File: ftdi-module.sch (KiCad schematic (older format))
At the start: 21 parts

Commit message: FTDI module complete
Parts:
- added 1V8_FT, 3V3, 5V0: TP_SMD1MM, antmicro-footprints:Testpoint_smd_1mm, symbol antmicroTestPoints:TP_SMD1MM
- added C? (x4): C_3u3_0402, antmicro-footprints:0402-cap, symbol antmicroCapacitors0402:C_3u3_0402
- added C? (x2): C_100n_0402, antmicro-footprints:0402-cap, symbol antmicroCapacitors0402:C_100n_0402
- added C? (x2): C_1u_0402, antmicro-footprints:0402-cap, symbol antmicroCapacitors0402:C_1u_0402
- added D?: PESD5V0S2BQA, antmicro-footprints:TPD2E009DRTR, symbol antmicroTVSDiodes:PESD5V0S2BQA
- added D?: KP-1608CGCK, antmicro-footprints:LED_0603, symbol antmicroLEDIndicationDiscrete:KP-1608CGCK
- added FB?: BLM18AG601SN1D, antmicro-footprints:0603, symbol antmicroFerriteBeadsandChips:BLM18AG601SN1D
- added J?: WE_629105150521, antmicro-footprints:USB_Micro_B_Female_629105150521, symbol antmicroUSBDVIHDMIConnectors:WE_629105150521
- added R?: R_0R_0603, antmicro-footprints:0603-res, symbol antmicroResistors0603:R_0R_0603
- added R?: R_330R_0402, antmicro-footprints:0402-res, symbol antmicroResistors0402:R_330R_0402
- added S?: MSS3-V-T_R, antmicro-footprints:Switch_Slide_MSS3, symbol antmicroSlideSwitches:MSS3-V-T_R
- added U?: NCP163ASN330T1G, antmicro-footprints:SOT-23-5, symbol antmicroPMICVoltageRegulatorsLinear:NCP163ASN330T1G
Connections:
- net GND: now also C?.2, C?.2, C?.2, C?.2, C?.2, C?.2, C?.2, C?.2, D?.2, D?.3 (GND), FB?.2, J?.5, U?.2 (GND)
- net VCC3V3: now also FB?.2, FB?.2, 3V3.1, C?.1, R?.1, U?.5 (VOUT)
- net 1V8_FT: now reaches U?.12 (VCORE-1), U?.37 (VCORE-2), U?.49 (VREGOUT), U?.64 (VCORE-3)
- net 1V8_FT: now also 1V8_FT.1, C?.1, C?.1, C?.1, C?.1, C?.1
- net USB_D-: now reaches U?.7 (DM)
- net USB_D-: now also D?.1 (IO1), J?.2
- new net: FB?.1, J?.6
- new net: C?.1, U?.1 (VIN)
- new net: D?.1, R?.2
- new net 3V3_EN: S?.2, U?.3 (EN)
- new net USB_D+: D?.2 (IO2), J?.3
- new net VBUS: C?.1, J?.1, R?.1, S?.1
- new net VCC5V0: 5V0.1, R?.2
- no-connect marks 0 -> 5
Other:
- note added: "3V3 LDO"
- note added: "FTDI"
- note added: "Power Filtering\n"
- note added: "Power LED"
- note added: "Power Switch\n"
- note added: "Probes"
- note added: "USB Connector\n"
- moved on the sheet: C?, FB?, R?, U?, Y?

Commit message: Small improvements. Power cycling module sheet
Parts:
- removed C? (x3): C_3u3_0402, antmicro-footprints:0402-cap, symbol antmicroCapacitors0402:C_3u3_0402
- added C? (x2): C_100n_0402, antmicro-footprints:0402-cap, symbol antmicroCapacitors0402:C_100n_0402
- gave numbers to parts that had none: 34
- renumbered 1V8_FT to 1V8_FT1
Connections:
- net 1V8_FT: now also C?.1, C?.1
- net GND: now also C?.2, C?.2
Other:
- moved on the sheet: C18, C19, U2

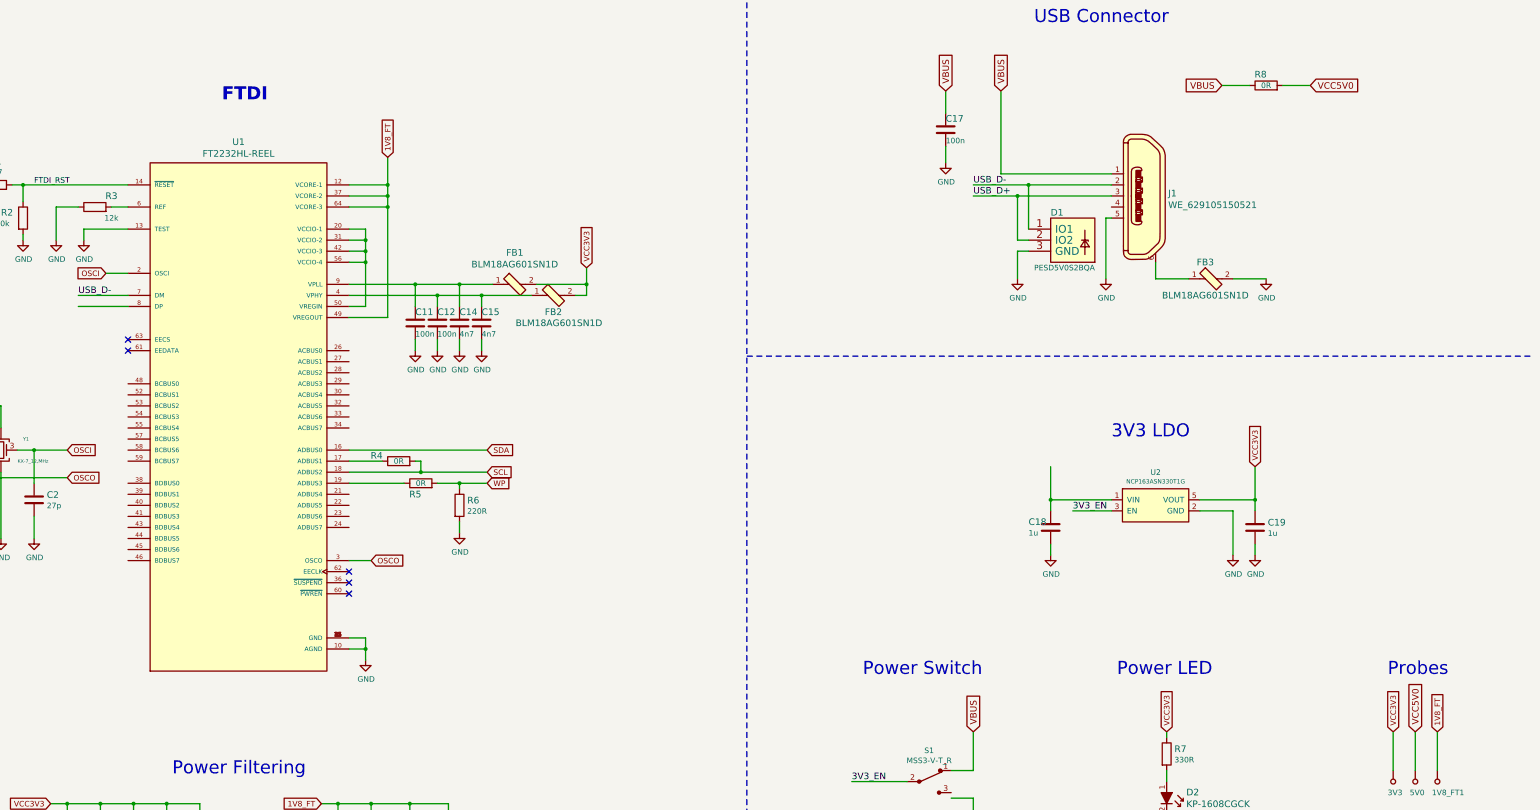
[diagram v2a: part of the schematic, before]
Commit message: Power cycling module update
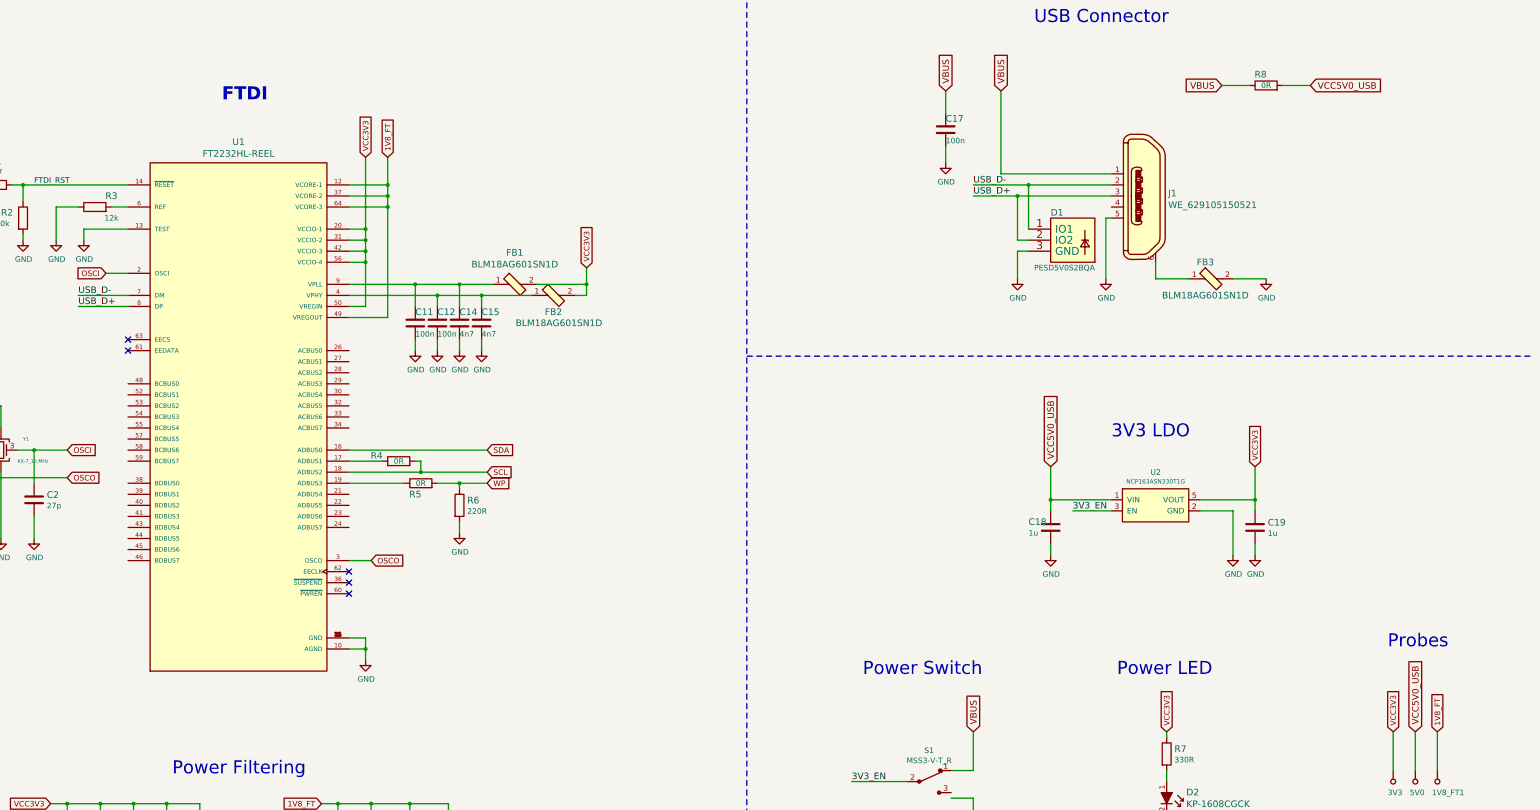
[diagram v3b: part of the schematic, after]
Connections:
- net VCC5V0 is gone; now on net VCC5V0_USB: 5V0.1, R8.2
- net USB_D+: now also U1.8 (DP)
- net VCC3V3: now also U1.20 (VCCIO-1), U1.31 (VCCIO-2), U1.42 (VCCIO-3), U1.50 (VREGIN), U1.56 (VCCIO-4)
- net VCC5V0_USB: now reaches C18.1, U2.1 (VIN)
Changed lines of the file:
@@
 VBUS
 Text GLabel 14050 1650 2    59   Input ~ 0
-VCC5V0
+VCC5V0_USB
 Wire Wire Line
 	14050 1650 13800 1650
@@
 Wire Wire Line
 	11700 5400 11700 5500
-Text GLabel 15000 7500 1    59   Input ~ 0
-VCC5V0
 Text GLabel 7500 3300 1    50   Input ~ 0
 VCC3V3
@@
 Wire Wire Line
 	12750 7850 12750 7950
-Text Notes 14750 7000 0    118  ~ 0
+Text Notes 14750 6750 0    118  ~ 0
 Probes
 Text GLabel 14800 7500 1    50   Input ~ 0
@@
 Wire Wire Line
 	11000 2650 11400 2650
+Text GLabel 11700 5100 1    59   Input ~ 0
+VCC5V0_USB
+Text GLabel 5500 2300 1    50   Input ~ 0
+VCC3V3
+Wire Wire Line
+	5500 2950 5500 2300
+Connection ~ 5500 2950
+Text Label 2900 3650 0    59   ~ 0
+USB_D+
+Text GLabel 15000 7500 1    59   Input ~ 0
+VCC5V0_USB
 $EndSCHEMATC

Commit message: Logic Shifter Module. Current Meas. implementation
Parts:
- added C? (x2): C_100n_0402, antmicro-footprints:0402-cap, symbol antmicroCapacitors0402:C_100n_0402
- added R? (x4): R_8k2_0402, antmicro-footprints:0402-res, symbol antmicroResistors0402:R_8k2_0402
- added R?: R_4k7_0402, antmicro-footprints:0402-res, symbol antmicroResistors0402:R_4k7_0402
- added SCL, SCL_3V3, SDA, SDA_3V3: TP_SMD1MM, antmicro-footprints:Testpoint_smd_1mm, symbol antmicroTestPoints:TP_SMD1MM
- added U?: TCA9406DC, symbol Interface:TCA9406DC
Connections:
- net GND: now also C?.2, C?.2, R?.2, U?.2 (GND)
- net SCL: now also R?.2, SCL.1, U?.8 (SCL_B); no longer R4.2, U1.18 (ADBUS2)
- net SDA: now also R?.2, SDA.1, U?.1 (SDA_B); no longer U1.16 (ADBUS0)
- net VCC3V3: now also C?.1, R?.1, R?.1, R?.1, U?.3 (VCCA), U?.6 (OE)
- new net SCL_3V3: R4.2, R?.2, SCL_3V3.1, U1.18 (ADBUS2), U?.5 (SCL_A)
- new net SDA_3V3: R?.2, SDA_3V3.1, U1.16 (ADBUS0), U?.4 (SDA_A)
- new net VCC5V0: C?.1, R?.1, R?.1, U?.7 (VCCB)
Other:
- note added: "Logic Level Shifter"
- note added: "Power filtering\n"
- note added: "To OE pin"
- moved on the sheet: 1V8_FT1, 3V3, 5V0, C1, C11, C12, C13, C14, C15, C2, C3, C4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

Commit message: Current Module upgrade. Logic unification.
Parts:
- removed 1V8_FT1, SCL_3V3, SDA_3V3: TP_SMD1MM, antmicro-footprints:Testpoint_smd_1mm, symbol antmicroTestPoints:TP_SMD1MM
- removed C? (x2): C_100n_0402, antmicro-footprints:0402-cap, symbol antmicroCapacitors0402:C_100n_0402
- removed R? (x4): R_8k2_0402, antmicro-footprints:0402-res, symbol antmicroResistors0402:R_8k2_0402
- removed R?: R_4k7_0402, antmicro-footprints:0402-res, symbol antmicroResistors0402:R_4k7_0402
- removed U?: TCA9406DC, symbol Interface:TCA9406DC
- added D? (x2): PMEG3005EH, Diode_SMD:D_SOD-123F, symbol Diode:PMEG3005EH
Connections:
- net SCL_3V3 is gone; now on net SCL: R4.2, U1.18 (ADBUS2)
- net SDA_3V3 is gone; now on net SDA: U1.16 (ADBUS0)
- net VCC5V0: now also 5V0.1, R8.2, D?.2 (A)
- net VCC5V0_USB: no longer names the net of C18.1, U2.1 (VIN)
- net VCC5V0_USB: no longer 5V0.1, R8.2
- new net: D?.1 (K), D?.1 (K)
- new net VCC12V0: D?.2 (A)
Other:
- note removed: "Logic Level Shifter"
- note removed: "Power filtering\n"
- note removed: "To OE pin"
- moved on the sheet: C18, C19, D2, R7, S1, SCL, SDA, U2
